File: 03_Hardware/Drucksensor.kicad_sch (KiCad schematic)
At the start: 96 parts, among them J101 24V in, J103 RS485-mini-1, J104 RJ45, J108 RJ45, J109 RJ45, J110 DS18B20, J111 BMP280, J112 RJ45, J113 RS485-mini-1, J114 AVR-ISP-6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

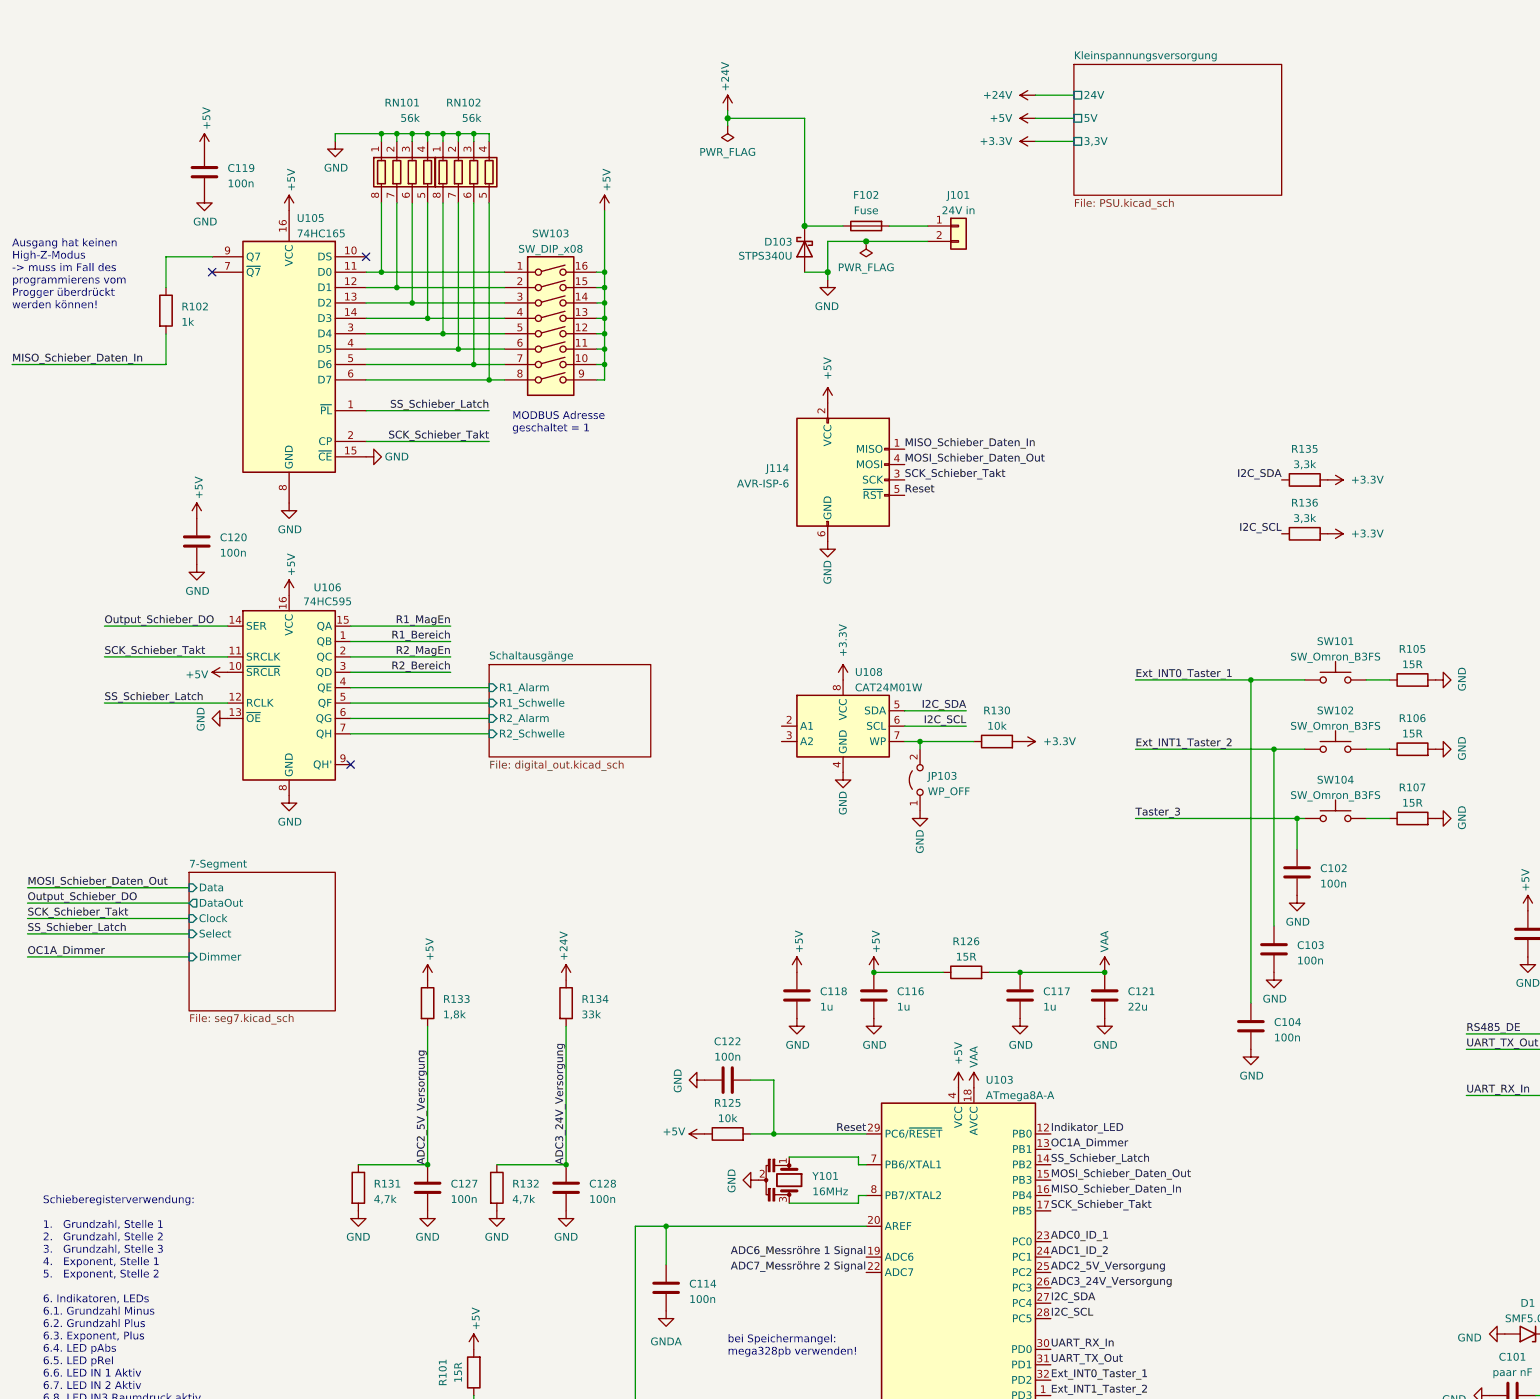
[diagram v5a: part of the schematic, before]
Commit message: Stecker fertig ausgewählt und Layout etwa 60% fertig
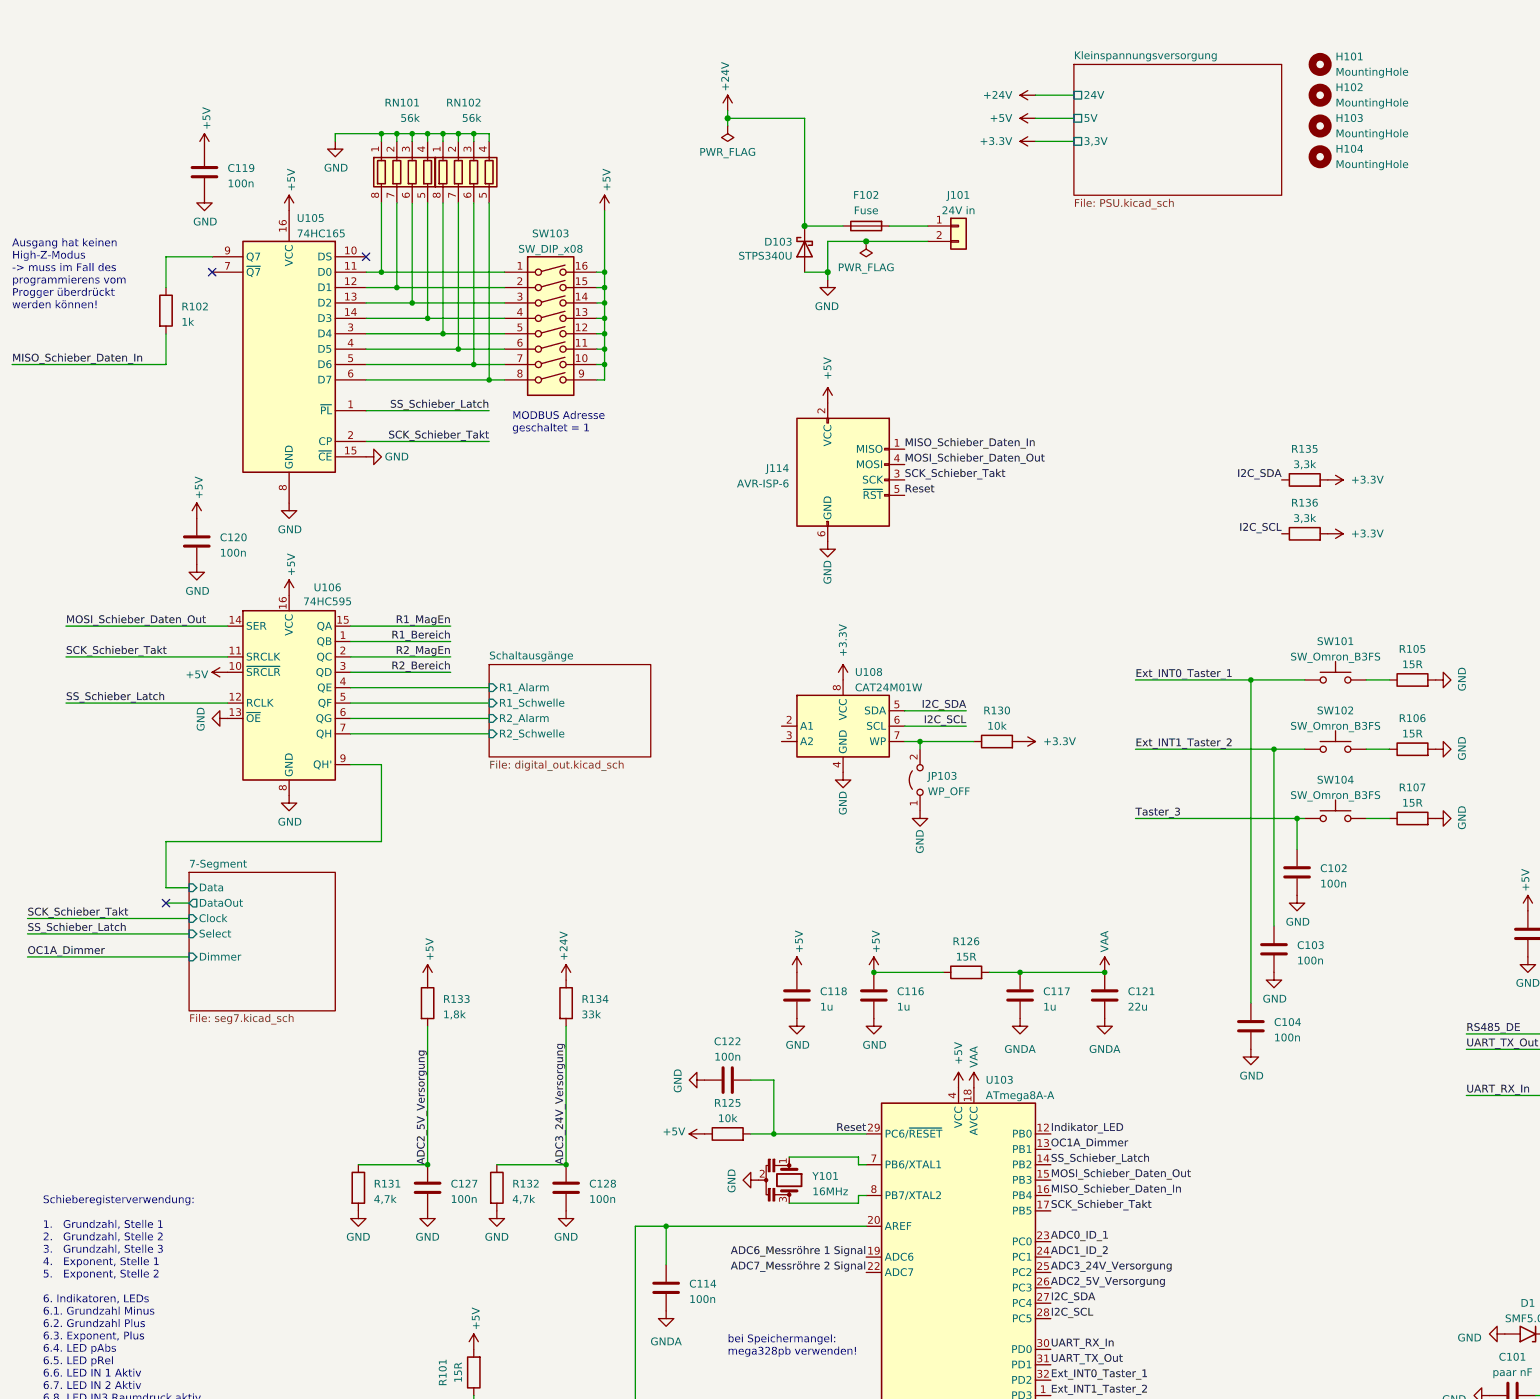
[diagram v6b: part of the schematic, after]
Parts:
- added H101, H102, H103, H104: MountingHole, MountingHole:MountingHole_3.2mm_M3_DIN965, symbol Mechanical:MountingHole
- J104, J108, J109, J112: footprint Sven:RJ45_Amphenol_54602_mod -> board:RJ45_Amphenol_54602_mod
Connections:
- net Output_Schieber_DO is gone; now on net MOSI_Schieber_Daten_Out: U106.14 (SER)
- net ADC2_5V_Versorgung: now also U103.26 (PC3); no longer U103.25 (PC2)
- net ADC3_24V_Versorgung: now also U103.25 (PC2); no longer U103.26 (PC3)
- net GND: no longer C117.2, C121.2
- net GNDA: now also C117.2, C121.2
- net 7-Segment/Data: now reaches U106.9 (QH')

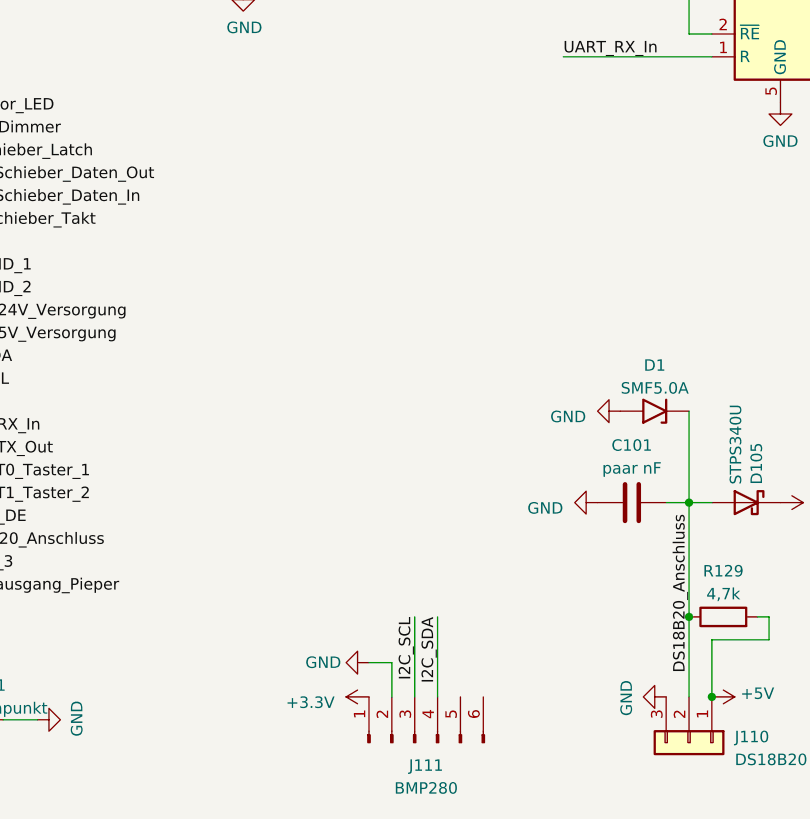
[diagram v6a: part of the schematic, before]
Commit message: Layout aktuell fast DRC-Fehlerfrei, Überlappungen von Plus-Zeichen sind in Ordnung. Texte müssen noch ausgerichtet werden!
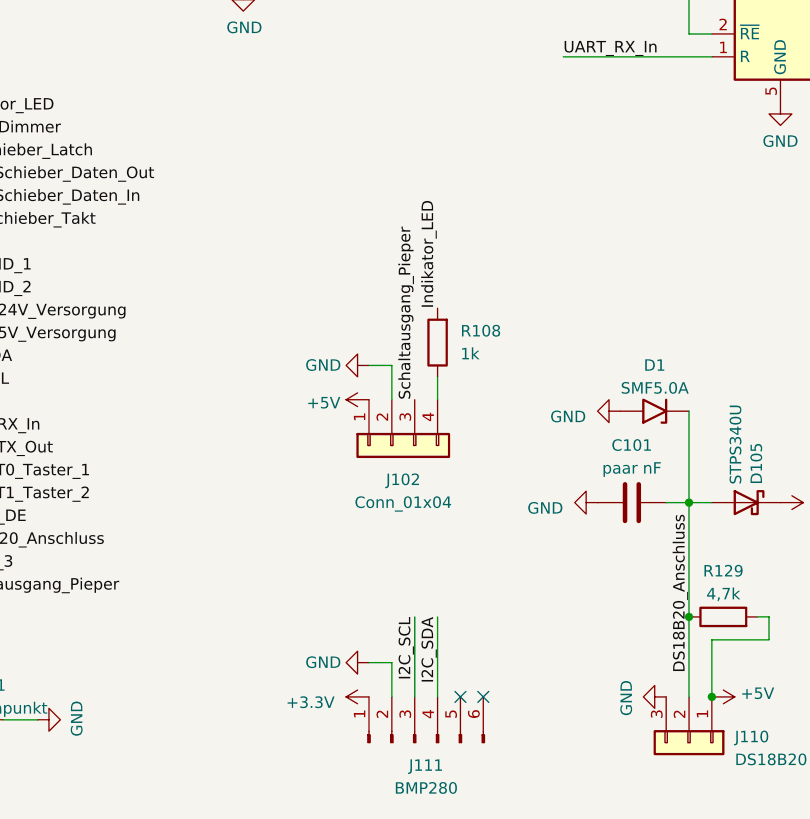
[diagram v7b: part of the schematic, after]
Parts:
- added J102: Conn_01x04, Connector_PinHeader_2.54mm:PinHeader_2x02_P2.54mm_Vertical, symbol Connector_Generic:Conn_01x04
- added R108: 1k, Resistor_SMD:R_0603_1608Metric, symbol Device:R
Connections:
- net +5V: now also J102.1 (Pin_1)
- net GND: now also J102.2 (Pin_2)
- net Indikator_LED: now also R108.2
- net Schaltausgang_Pieper: now also J102.3 (Pin_3)
- new net: J102.4 (Pin_4), R108.1
- no-connect marks 9 -> 11
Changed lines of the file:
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@@
   (no_connect (at 48.26 163.83))
   (no_connect (at 378.46 55.88))
+  (no_connect (at 254 266.7))
   (no_connect (at 378.46 50.8))
   (no_connect (at 378.46 110.49))
   (no_connect (at 378.46 105.41))
+  (no_connect (at 251.46 266.7))
   (wire (pts (xy 316.23 100.33) (xy 317.5 100.33))
     (stroke (width 0) (type default))
@@
     (stroke (width 0) (type default))
   )
+  (wire (pts (xy 241.3 229.87) (xy 243.84 229.87))
+    (stroke (width 0) (type default))
+  )
   (wire (pts (xy 120.65 64.77) (xy 120.65 67.31))
     (stroke (width 0) (type default))
@@
     (stroke (width 0) (type default))
   )
+  (wire (pts (xy 243.84 229.87) (xy 243.84 233.68))
+    (stroke (width 0) (type default))
+  )
   (wire (pts (xy 120.65 59.69) (xy 120.65 62.23))
     (stroke (width 0) (type default))
@@
     (stroke (width 0) (type default))
   )
+  (wire (pts (xy 248.92 231.14) (xy 248.92 233.68))
+    (stroke (width 0) (type default))
+  )
   (wire (pts (xy 83.82 140.97) (xy 83.82 153.67))
     (stroke (width 0) (type default))
@@
     (effects (font (size 1.27 1.27)) (justify left bottom))
   )
+  (label "Indikator_LED" (at 248.92 223.52 90) (fields_autoplaced)
+    (effects (font (size 1.27 1.27)) (justify left bottom))
+  )
   (label "ADC2_5V_Versorgung" (at 91.44 207.01 90) (fields_autoplaced)
     (effects (font (size 1.27 1.27)) (justify left bottom))
@@
     (effects (font (size 1.27 1.27)) (justify left bottom))
   )
+  (label "Schaltausgang_Pieper" (at 246.38 233.68 90) (fields_autoplaced)
+    (effects (font (size 1.27 1.27)) (justify left bottom))
+  )
   (label "SCK_Schieber_Takt" (at 25.4 166.37 0) (fields_autoplaced)
     (effects (font (size 1.27 1.27)) (justify left bottom))
@@
     )
   )
+  (symbol (lib_id "Connector_Generic:Conn_01x04") (at 243.84 238.76 90) (mirror x) (unit 1)
+    (in_bom yes) (on_board yes) (dnp no) (fields_autoplaced)
+    (property "Reference" "J102" (at 245.11 242.57 90)
+      (effects (font (size 1.27 1.27)))
+    )
+    (property "Value" "Conn_01x04" (at 245.11 245.11 90)
+      (effects (font (size 1.27 1.27)))
+    )
+    (property "Footprint" "Connector_PinHeader_2.54mm:PinHeader_2x02_P2.54mm_Vertical" (at 243.84 238.76 0)
+      (effects (font (size 1.27 1.27)) hide)
+    )
+    (property "Datasheet" "~" (at 243.84 238.76 0)
+      (effects (font (size 1.27 1.27)) hide)
+    )
+    (pin "2")
+    (pin "4")
+    (pin "3")
+    (pin "1")
+    (instances
+      (project "Drucksensor"
+        (path "/d772951a-27ae-4d3f-b561-d53c012cef6f"
+          (reference "J102") (unit 1)
+        )
+      )
+    )
+  )
   (symbol (lib_id "power:GND") (at 274.32 266.7 270) (unit 1)
     (in_bom yes) (on_board yes) (dnp no)
@@
     )
   )
+  (symbol (lib_id "power:GND") (at 241.3 229.87 270) (unit 1)
+    (in_bom yes) (on_board yes) (dnp no)
+    (property "Reference" "#PWR0124" (at 234.95 229.87 0)
+      (effects (font (size 1.27 1.27)) hide)
+    )
+    (property "Value" "GND" (at 236.22 229.87 90)
+      (effects (font (size 1.27 1.27)))
+    )
+    (property "Footprint" "" (at 241.3 229.87 0)
+      (effects (font (size 1.27 1.27)) hide)
+    )
+    (property "Datasheet" "" (at 241.3 229.87 0)
+      (effects (font (size 1.27 1.27)) hide)
+    )
+    (pin "1")
+    (instances
+      (project "Drucksensor"
+        (path "/d772951a-27ae-4d3f-b561-d53c012cef6f"
+          (reference "#PWR0124") (unit 1)
+        )
+      )
+    )
+  )
   (symbol (lib_id "power:GND") (at 54.61 46.99 0) (unit 1)
     (in_bom yes) (on_board yes) (dnp no)
@@
     )
   )
+  (symbol (lib_id "Device:R") (at 248.92 227.33 180) (unit 1)
+    (in_bom yes) (on_board yes) (dnp no) (fields_autoplaced)
+    (property "Reference" "R108" (at 251.46 226.06 0)
+      (effects (font (size 1.27 1.27)) (justify right))
+    )
+    (property "Value" "1k" (at 251.46 228.6 0)
+      (effects (font (size 1.27 1.27)) (justify right))
+    )
+    (property "Footprint" "Resistor_SMD:R_0603_1608Metric" (at 250.698 227.33 90)
+      (effects (font (size 1.27 1.27)) hide)
+    )
+    (property "Datasheet" "~" (at 248.92 227.33 0)
+      (effects (font (size 1.27 1.27)) hide)
+    )
+    (pin "1")
+    (pin "2")
+    (instances
+      (project "Drucksensor"
+        (path "/d772951a-27ae-4d3f-b561-d53c012cef6f"
+          (reference "R108") (unit 1)
+        )
+      )
+    )
+  )
   (symbol (lib_id "Device:R_Pack04") (at 88.9 43.18 0) (mirror x) (unit 1)
     (in_bom yes) (on_board yes) (dnp no)
@@
         )
       )
+    )
+  )
+  (symbol (lib_id "power:+5V") (at 241.3 233.68 90) (mirror x) (unit 1)
+    (in_bom yes) (on_board yes) (dnp no)
+    (property "Reference" "#PWR0153" (at 245.11 233.68 0)
+      (effects (font (size 1.27 1.27)) hide)
+    )
+    (property "Value" "+5V" (at 238.1249 234.0483 90)
+      (effects (font (size 1.27 1.27)) (justify left))
+    )
+    (property "Footprint" "" (at 241.3 233.68 0)
+      (effects (font (size 1.27 1.27)) hide)
+    )
+    (property "Datasheet" "" (at 241.3 233.68 0)
+      (effects (font (size 1.27 1.27)) hide)
+    )
+    (pin "1")
+    (instances
+      (project "Drucksensor"
+        (path "/d772951a-27ae-4d3f-b561-d53c012cef6f"
+          (reference "#PWR0153") (unit 1)
+        )
+      )

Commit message: Software weitergemacht
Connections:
- net GND: now also U108.2 (A1), U108.3 (A2)
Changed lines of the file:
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@@
+    )
+  )
+  (symbol (lib_id "power:GND") (at 149.86 134.62 270) (unit 1)
+    (in_bom yes) (on_board yes) (dnp no)
+    (property "Reference" "#PWR0155" (at 143.51 134.62 0)
+      (effects (font (size 1.27 1.27)) hide)
+    )
+    (property "Value" "GND" (at 144.78 134.62 90)
+      (effects (font (size 1.27 1.27)))
+    )
+    (property "Footprint" "" (at 149.86 134.62 0)
+      (effects (font (size 1.27 1.27)) hide)
+    )
+    (property "Datasheet" "" (at 149.86 134.62 0)
+      (effects (font (size 1.27 1.27)) hide)
+    )
+    (pin "1")
+    (instances
+      (project "Drucksensor"
+        (path "/d772951a-27ae-4d3f-b561-d53c012cef6f"
+          (reference "#PWR0155") (unit 1)
+        )
+      )
     )
   )
@@
         )
       )
+    )
+  )
+  (symbol (lib_id "power:GND") (at 149.86 137.16 270) (unit 1)
+    (in_bom yes) (on_board yes) (dnp no)
+    (property "Reference" "#PWR0154" (at 143.51 137.16 0)
+      (effects (font (size 1.27 1.27)) hide)
+    )
+    (property "Value" "GND" (at 144.78 137.16 90)
+      (effects (font (size 1.27 1.27)))
+    )
+    (property "Footprint" "" (at 149.86 137.16 0)
+      (effects (font (size 1.27 1.27)) hide)
+    )
+    (property "Datasheet" "" (at 149.86 137.16 0)
+      (effects (font (size 1.27 1.27)) hide)
+    )
+    (pin "1")
+    (instances
+      (project "Drucksensor"
+        (path "/d772951a-27ae-4d3f-b561-d53c012cef6f"
+          (reference "#PWR0154") (unit 1)
+        )
+      )
